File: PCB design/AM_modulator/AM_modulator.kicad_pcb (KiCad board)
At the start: 2 copper layers, 11 parts, among them Q1 MMBT3904

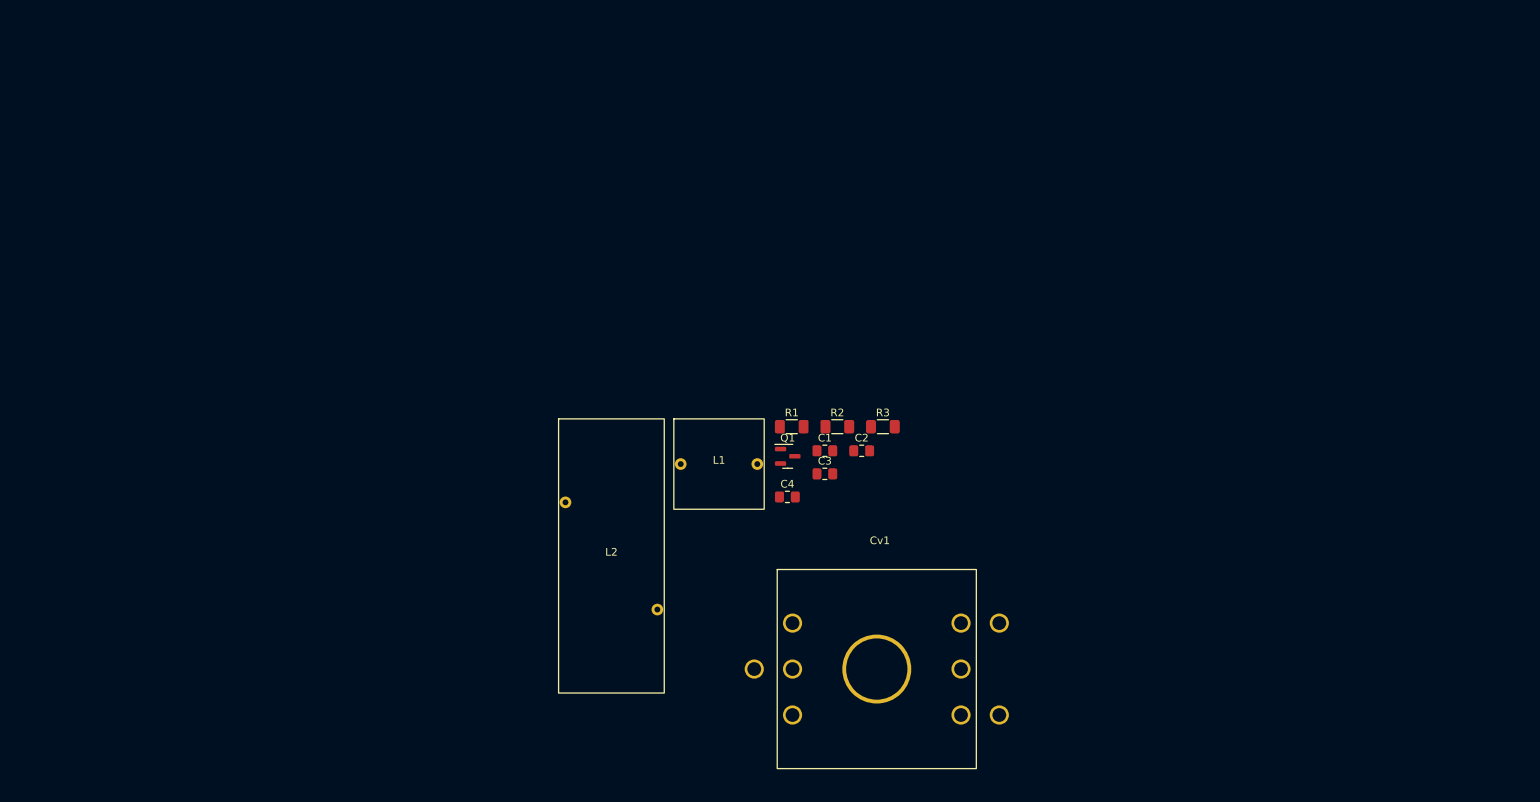
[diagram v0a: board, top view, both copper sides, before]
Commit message: oscillator PCB design done
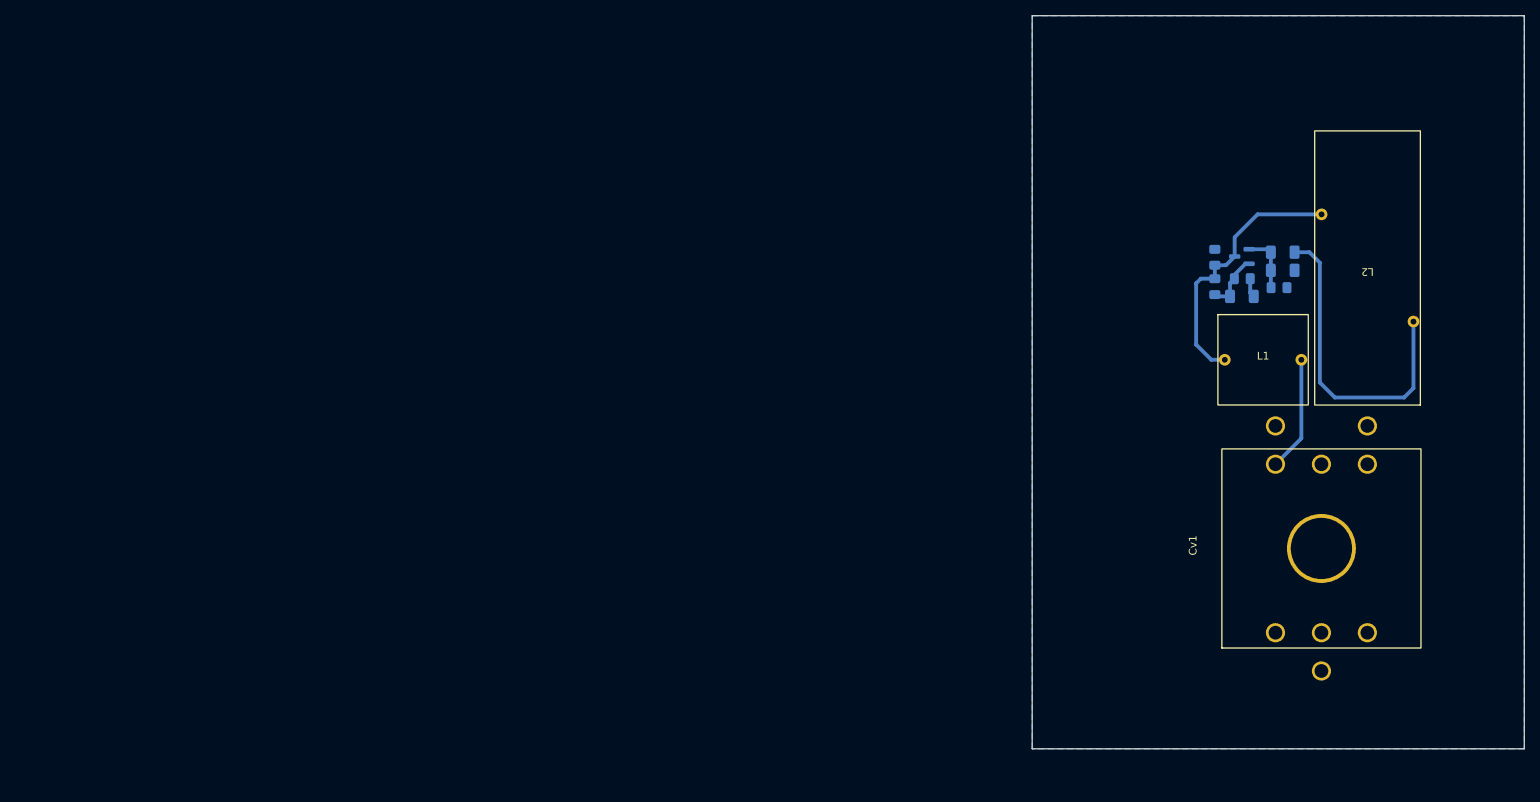
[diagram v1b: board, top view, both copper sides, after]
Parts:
- C1, C2, C3, C4, Q1, R1, R2, R3: moved to B.Cu
- moved L2 105.7 mm to (215.5, 62.8), turned to 180 degrees
- moved L1 72.3 mm to (201.9, 74.8)
- moved R1 68.0 mm to (204.5, 60.7), turned to 180 degrees
- moved Q1 64.8 mm to (199.1, 61.3), turned to 180 degrees
- moved C3 64.1 mm to (204.0, 65.4)
- moved C4 64.0 mm to (195.6, 61.4), turned to 90 degrees
- moved R2 61.6 mm to (204.5, 63.1)
- moved Cv1 60.2 mm to (209.5, 99.4), turned to 90 degrees
- moved C1 55.3 mm to (195.6, 65.2), turned to -90 degrees
- moved C2 54.5 mm to (199.2, 64.2)
- moved R3 49.9 mm to (199.1, 66.5)
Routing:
- net +10V: track 0.00 -> 41.7 mm
- net Net-(C1-Pad1): track 0.00 -> 35.2 mm
- net Net-(Cv1-Pad1): track 0.00 -> 15.0 mm
- net Net-(C3-Pad1): track 0.00 -> 7.64 mm
- net Net-(C1-Pad2): track 0.00 -> 7.64 mm
- net GND: track 0.00 -> 2.50 mm
- added copper zone on B.Cu, net GND
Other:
- board outline added: 64.3 x 95.7 mm

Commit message: Avances placa
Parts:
- added Antena+1: Conn_01x01_Female, Connector_Pin:Pin_D1.4mm_L8.5mm_W2.8mm_FlatFork, F.Cu at (120.5, 63.7)
- added Antena-1: Conn_01x01_Female, Connector_Pin:Pin_D1.4mm_L8.5mm_W2.8mm_FlatFork, F.Cu at (120.3, 116.4)
- added CMLO1: 100n, Capacitor_SMD:C_0805_2012Metric_Pad1.18x1.45mm_HandSolder, B.Cu at (141.9, 67.5)
- added CMa1: 100n, Capacitor_SMD:C_0805_2012Metric_Pad1.18x1.45mm_HandSolder, B.Cu at (136.8, 70.3)
- added CMan1: 33p, Capacitor_SMD:C_0805_2012Metric_Pad1.18x1.45mm_HandSolder, B.Cu at (132.9, 69.7)
- added Cpi1: C, Capacitor_SMD:C_0805_2012Metric_Pad1.18x1.45mm_HandSolder, B.Cu at (128.7, 69.8)
- added Cpi11: C, Capacitor_SMD:C_0805_2012Metric_Pad1.18x1.45mm_HandSolder, B.Cu at (126.3, 69.9)
- added Cpi2: C, Capacitor_SMD:C_0805_2012Metric_Pad1.18x1.45mm_HandSolder, B.Cu at (128.7, 65.5)
- added Cpi21: C, Capacitor_SMD:C_0805_2012Metric_Pad1.18x1.45mm_HandSolder, B.Cu at (126.3, 65.5)
- added J1: AudioJack3, Jack Sigma:Jack_Sigma, B.Cu at (117.4, 103.9)
- added J2: Conn_01x02_Female, Connector_PinSocket_2.54mm:PinSocket_1x02_P2.54mm_Vertical, F.Cu at (110.9, 66.0)
- added Lpi1: L, Inductor_THT:L_Toroid_Vertical_L21.6mm_W9.1mm_P8.40mm_Bourns_5700, F.Cu at (109.9, 85.0)
- added QM1: MMBT3904, Package_TO_SOT_SMD:SOT-23, B.Cu at (136.8, 66.5)
- added RMb1: 100k, Resistor_SMD:R_1206_3216Metric_Pad1.30x1.75mm_HandSolder, B.Cu at (141.9, 65.0)
- added RMb2: 100k, Resistor_SMD:R_1206_3216Metric_Pad1.30x1.75mm_HandSolder, B.Cu at (141.9, 61.5)
- added RMc1: 220, Resistor_SMD:R_0805_2012Metric_Pad1.20x1.40mm_HandSolder, B.Cu at (133.0, 65.6)
- added RMe1: 100, Resistor_SMD:R_1206_3216Metric_Pad1.30x1.75mm_HandSolder, B.Cu at (142.0, 70.2)
- moved Cv1 68.3 mm to (141.9, 109.5), turned to 180 degrees
- moved C1 64.5 mm to (133.0, 80.5)
- moved C2 64.5 mm to (136.6, 79.4)
- moved C3 64.5 mm to (141.4, 80.6)
- moved C4 64.5 mm to (133.0, 76.7)
- moved L1 64.5 mm to (139.3, 90.0)
- moved L2 64.5 mm to (152.9, 78.0)
- moved Q1 64.5 mm to (136.5, 76.6)
- moved R1 64.5 mm to (141.8, 76.0)
- moved R2 64.5 mm to (141.8, 78.4)
- moved R3 64.5 mm to (136.5, 81.8)
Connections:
- C4 pad 2: /clapp_oscillator/Vout_30MHz_50Ohm -> /Mixer/LO
- L2 pad 1: +10V -> +12V
- R1 pad 1: +10V -> Net-(C1-Pad1)
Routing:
- net +10V: track 41.7 -> 0.00 mm
- net /Mixer/LO: track 0.00 -> 20.8 mm
- net /Antenna/RF_Antenna: track 0.00 -> 19.2 mm
- net Net-(Cv1-Pad1): track 15.0 -> 0.00 mm
- net Net-(CMLO1-Pad1): track 0.00 -> 9.09 mm
- net Net-(Antena+1-Pad1): track 0.00 -> 8.60 mm
- net Net-(CMa1-Pad1): track 0.00 -> 5.74 mm
- removed copper zone on B.Cu, net GND
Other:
- board size 64.3 x 95.7 mm -> 54.4 x 64.5 mm

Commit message: Placa terminada
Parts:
- removed CMan1: 33p, Capacitor_SMD:C_0805_2012Metric_Pad1.18x1.45mm_HandSolder
- added J3: SMA_CONNECTOR, SMA_T:LPRS_SMA_CONNECTOR, F.Cu at (123.0, 91.9)
- added J4: SMA_CONNECTOR, SMA_T:LPRS_SMA_CONNECTOR, F.Cu at (123.0, 82.5)
- moved Lpi1 16.6 mm to (120.4, 72.1), turned to 0 degrees
- moved J2 3.24 mm to (113.5, 64.0)
- moved Antena-1 2.71 mm to (121.9, 118.6)
- moved J1 2.14 mm to (117.8, 106.0)
- moved Cpi11 1.28 mm to (127.5, 69.8)
- moved Cpi21 1.28 mm to (127.5, 65.4)
- moved Cpi1 1.28 mm to (130.0, 69.8)
- moved Cpi2 1.28 mm to (130.0, 65.5)
- moved RMb2 0.99 mm to (141.9, 62.5)
- moved Antena+1 0.69 mm to (120.6, 64.4)
- moved CMLO1 0.47 mm to (142.0, 67.9)
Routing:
- net +12V: track 0.00 -> 74.2 mm
- net /Mixer/Audio: track 0.00 -> 52.8 mm
- net Net-(Cv1-Pad1): track 0.00 -> 35.2 mm
- net /Mixer/LO: track 20.8 -> 42.9 mm
- net /Antenna/RF_Antenna: track 19.2 -> 29.2 mm
- net Net-(Antena+1-Pad1): track 8.60 -> 13.7 mm
- net Net-(CMLO1-Pad1): track 9.09 -> 8.12 mm
- added copper zone on B.Cu, net GND
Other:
- board size 54.4 x 64.5 mm -> 51.5 x 64 mm

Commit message: PCB 2.0
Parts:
- added SW1: SW_DIP_x01, Resistor_SMD:R_0603_1608Metric_Pad0.98x0.95mm_HandSolder, B.Cu at (136.8, 83.3)
- added SW2: SW_DIP_x01, Resistor_SMD:R_0603_1608Metric_Pad0.98x0.95mm_HandSolder, B.Cu at (146.2, 83.2)
- added SW3: SW_DIP_x01, Resistor_SMD:R_0603_1608Metric_Pad0.98x0.95mm_HandSolder, B.Cu at (136.8, 85.3)
- added SW4: SW_DIP_x01, Resistor_SMD:R_0603_1608Metric_Pad0.98x0.95mm_HandSolder, B.Cu at (146.2, 85.3)
- moved J2 49.2 mm to (162.1, 72.4), turned to -90 degrees
- moved RMb2 44.0 mm to (163.6, 100.7), turned to -90 degrees
- moved Antena+1 43.3 mm to (161.5, 78.7), turned to -90 degrees
- moved Antena-1 40.5 mm to (107.5, 80.7), turned to -90 degrees
- moved RMb1 40.5 mm to (161.1, 100.7), turned to 90 degrees
- moved Cpi21 38.3 mm to (161.0, 84.2), turned to 0 degrees
- moved RMc1 38.0 mm to (160.5, 91.8), turned to 180 degrees
- moved CMLO1 37.8 mm to (156.9, 102.6), turned to 180 degrees
- moved Cpi2 37.5 mm to (160.9, 86.6), turned to 0 degrees
- moved QM1 37.0 mm to (159.6, 95.6), turned to 90 degrees
- moved CMa1 35.1 mm to (156.9, 99.1)
- moved L2 34.0 mm to (148.1, 111.8), turned to 90 degrees
- moved Lpi1 33.6 mm to (153.3, 78.4), turned to -90 degrees
- moved Cpi11 32.4 mm to (156.6, 84.2), turned to 0 degrees
- moved Cpi1 31.5 mm to (156.6, 86.6), turned to 180 degrees
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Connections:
- C4 pad 2: /Mixer/LO -> Net-(C4-Pad2)
- J3 pad 1: /Mixer/LO -> /clapp_oscillator/Vout_30MHz_50Ohm
- J4 pad 1: /Antenna/RF_Antenna -> /Mixer/RF
- QM1 pad 3: /Antenna/RF_Antenna -> Net-(QM1-Pad3)
- RMc1 pad 2: /Antenna/RF_Antenna -> Net-(QM1-Pad3)
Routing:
- net Net-(QM1-Pad3): track 0.00 -> 18.1 mm
- net Net-(C4-Pad2): track 0.00 -> 17.6 mm
- net /clapp_oscillator/Vout_30MHz_50Ohm: track 0.00 -> 9.69 mm
- net /Antenna/RF_Antenna: track 29.2 -> 19.5 mm
- net /Mixer/LO: track 42.9 -> 33.3 mm
- net /Mixer/RF: track 0.00 -> 9.19 mm
- net Net-(CMLO1-Pad1): track 8.12 -> 11.2 mm
- net Net-(C1-Pad1): track 35.2 -> 34.0 mm
- net +12V: track 74.2 -> 75.2 mm
- net /Mixer/Audio: track 52.8 -> 52.0 mm
- net Net-(Antena+1-Pad1): track 13.7 -> 12.9 mm
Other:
- board size 51.5 x 64 mm -> 64 x 51.5 mm

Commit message: PCB design done
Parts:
- removed Cv1: 30p, capacitors:variable_cap
- removed L2: 10u, inductors:T-130
- added C5: 100n, Capacitor_SMD:C_0805_2012Metric_Pad1.18x1.45mm_HandSolder, B.Cu at (109.0, 126.7)
- C1: value 1n -> 220p
- C2: value 10n -> 220p
- Cpi1, Cpi11: value C -> 220p
- Cpi2, Cpi21: value C -> 33p
- L1: value 938.16n -> 250n
- Lpi1: value L -> 551.6nH
- R1: value 6.8k -> 10k
- R2: value 3.3k -> 15k
- R3: value 68 -> 470
- SW1, SW2, SW3, SW4: footprint Resistor_SMD:R_0603_1608Metric_Pad0.98x0.95mm_HandSolder -> Resistor_SMD:R_1206_3216Metric
- moved J2 72.4 mm to (115.8, 128.1), turned to 90 degrees
- moved RMc1 60.1 mm to (111.5, 126.7), turned to 90 degrees
- moved QM1 53.2 mm to (112.6, 120.6), turned to 180 degrees
- moved C2 52.2 mm to (101.4, 122.2), turned to 180 degrees
- moved SW2 51.4 mm to (103.4, 111.8)
- moved C3 51.1 mm to (100.8, 125.7)
- moved R2 50.7 mm to (103.5, 126.2)
- moved Q1 50.5 mm to (105.8, 121.3)
- moved L1 50.5 mm to (92.3, 123.2)
- moved R1 50.3 mm to (106.3, 126.2)
- moved R3 49.3 mm to (101.0, 119.6), turned to 180 degrees
- moved CMa1 48.9 mm to (114.6, 123.6), turned to 0 degrees
- moved J3 48.4 mm to (96.7, 107.1)
- moved J1 48.3 mm to (128.2, 124.3), turned to 90 degrees
- moved RMb2 48.3 mm to (117.6, 115.4), turned to 0 degrees
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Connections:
- net /Mixer/Audio renamed /audio
- C2 pad 2: GND -> Net-(C2-Pad2)
- C4 pad 2: Net-(C4-Pad2) -> /SMA_probe/signal_in
- J3 pad 1: /clapp_oscillator/Vout_30MHz_50Ohm -> Net-(SW1-Pad2)
- J4 pad 1: /Mixer/RF -> Net-(SW3-Pad2)
- L1 pad 2: Net-(Cv1-Pad1) -> Net-(C2-Pad2)
- QM1 pad 3: Net-(QM1-Pad3) -> /Mixer/RF
- R1 pad 1: Net-(C1-Pad1) -> +12V
- RMc1 pad 2: Net-(QM1-Pad3) -> /Mixer/RF
- SW1 pad 1: /clapp_oscillator/Vout_30MHz_50Ohm -> /SMA_probe/signal_in
- SW1 pad 2: /Mixer/LO -> Net-(SW1-Pad2)
- SW2 pad 1: /Mixer/RF -> Net-(SW1-Pad2)
- SW2 pad 2: /Antenna/RF_Antenna -> /Mixer/LO
- SW3 pad 1: Net-(C4-Pad2) -> /Mixer/RF
- SW3 pad 2: /clapp_oscillator/Vout_30MHz_50Ohm -> Net-(SW3-Pad2)
- SW4 pad 1: Net-(QM1-Pad3) -> Net-(SW3-Pad2)
- SW4 pad 2: /Mixer/RF -> /Antenna/RF_Antenna
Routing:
- net /audio: track 52.0 -> 4.08 mm
- net Net-(Cv1-Pad1): track 35.2 -> 0.00 mm
- net +12V: track 75.2 -> 40.1 mm
- net /Mixer/LO: track 33.3 -> 10.8 mm
- net Net-(QM1-Pad3): track 18.1 -> 0.00 mm
- net Net-(C4-Pad2): track 17.6 -> 0.00 mm
- net Net-(C2-Pad2): track 0.00 -> 13.1 mm
- net Net-(SW3-Pad2): track 0.00 -> 12.5 mm
- net Net-(SW1-Pad2): track 0.00 -> 12.0 mm
- net Net-(C1-Pad1): track 34.0 -> 22.2 mm
- net /clapp_oscillator/Vout_30MHz_50Ohm: track 9.69 -> 0.00 mm
- net /SMA_probe/signal_in: track 0.00 -> 6.84 mm
- net Net-(CMLO1-Pad1): track 11.2 -> 7.52 mm
- net /Antenna/RF_Antenna: track 19.5 -> 16.3 mm
- net GND: track 2.50 -> 0.00 mm
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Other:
- board size 64 x 51.5 mm -> 50 x 27.4 mm

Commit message: PCB design done
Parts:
- L1: footprint inductors:air_core_1cm -> inductors:variable_inductor
- RMc1: value 220 -> 240; footprint Resistor_SMD:R_0805_2012Metric_Pad1.20x1.40mm_HandSolder -> Resistor_SMD:R_1206_3216Metric_Pad1.30x1.75mm_HandSolder
- moved RMc1 66.0 mm to (74.5, 72.0)
- moved L1 65.7 mm to (56.0, 68.5), turned to 90 degrees
- moved C5 65.6 mm to (71.9, 72.6)
- moved C2 65.6 mm to (64.3, 68.2)
- moved C4 65.6 mm to (71.9, 64.7)
- moved R1 65.6 mm to (69.2, 72.1)
- moved R2 65.6 mm to (66.4, 72.1)
- moved SW1 65.6 mm to (66.3, 60.5)
- moved SW2 65.6 mm to (66.3, 57.8)
- moved C1 65.6 mm to (68.6, 63.9)
- moved C3 65.6 mm to (63.7, 71.7)
- moved J1 65.6 mm to (91.1, 70.2)
- moved J2 65.6 mm to (78.7, 74.0)
- moved Q1 65.6 mm to (68.7, 67.3)
- moved R3 65.6 mm to (63.9, 65.6)
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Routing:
- net Net-(C2-Pad2): track 13.1 -> 6.70 mm
- net /Mixer/RF: track 11.0 -> 7.53 mm
- net Net-(C1-Pad1): track 22.2 -> 19.1 mm
- net +12V: track 40.1 -> 37.9 mm
- net Net-(J3-Pad1): track 12.0 -> 9.83 mm
- net Net-(J4-Pad1): track 12.5 -> 10.8 mm
- net Net-(Antena+1-Pad1): track 13.2 -> 11.7 mm
- net /Antenna/RF_Antenna: track 16.3 -> 17.5 mm
- net /SMA_probe/signal_in: track 6.84 -> 6.08 mm
- net /audio: track 4.08 -> 3.51 mm
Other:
- board size 50 x 27.4 mm -> 50 x 25 mm

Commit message: PCB corregida
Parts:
- R3: value 470 -> 430
- moved J2 3.83 mm to (75.0, 73.0)
- moved CMa1 3.40 mm to (75.0, 69.0)
- moved Antena+1 3.38 mm to (92.2, 54.8)
- moved C1 3.38 mm to (65.4, 62.8)
- moved Cpi21 3.38 mm to (91.9, 59.5)
- moved SW3 3.38 mm to (71.4, 61.0)
- moved SW4 3.38 mm to (77.2, 56.5)
- moved C3 3.38 mm to (60.5, 70.5)
- moved R3 3.38 mm to (60.7, 64.5)
- moved Antena-1 3.38 mm to (48.5, 55.0)
- moved L1 3.38 mm to (52.7, 67.4)
- moved C4 3.38 mm to (68.7, 63.6)
- moved CMLO1 3.38 mm to (74.0, 62.0)
- moved Cpi1 3.38 mm to (86.0, 61.2)
- moved Cpi2 3.38 mm to (91.9, 62.0)
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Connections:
- C2 pad 2: Net-(C2-Pad2) -> +12V
- L1 pad 2: Net-(C2-Pad2) -> +12V
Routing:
- net +12V: track 37.9 -> 59.5 mm
- net Net-(C2-Pad2): track 6.70 -> 0.00 mm
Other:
- board size 50 x 25 mm -> 50 x 26.3 mm
